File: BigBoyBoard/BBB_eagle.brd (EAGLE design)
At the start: 94 x 87.1 mm, 36 parts, among them Y2 ECS-80-S-4X

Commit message: 1/1 review
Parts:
- moved U$6 1.60 mm to (47.0, 78.7)
- moved U$4 0.83 mm to (46.5, 7.40)
- moved RSH2 0.61 mm to (39.0, 50.7)
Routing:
- net +5VGND: track 167.9 -> 158.1 mm
- net +5V: track 168.8 -> 159.0 mm
- net +12V: track 244.4 -> 237.5 mm
- net GND: track 136.6 -> 134.0 mm, vias 30 -> 31
- net GNDA: track 185.7 -> 183.2 mm
- net +3V3: track 203.9 -> 202.6 mm
- net VCC2: track 27.6 -> 28.2 mm

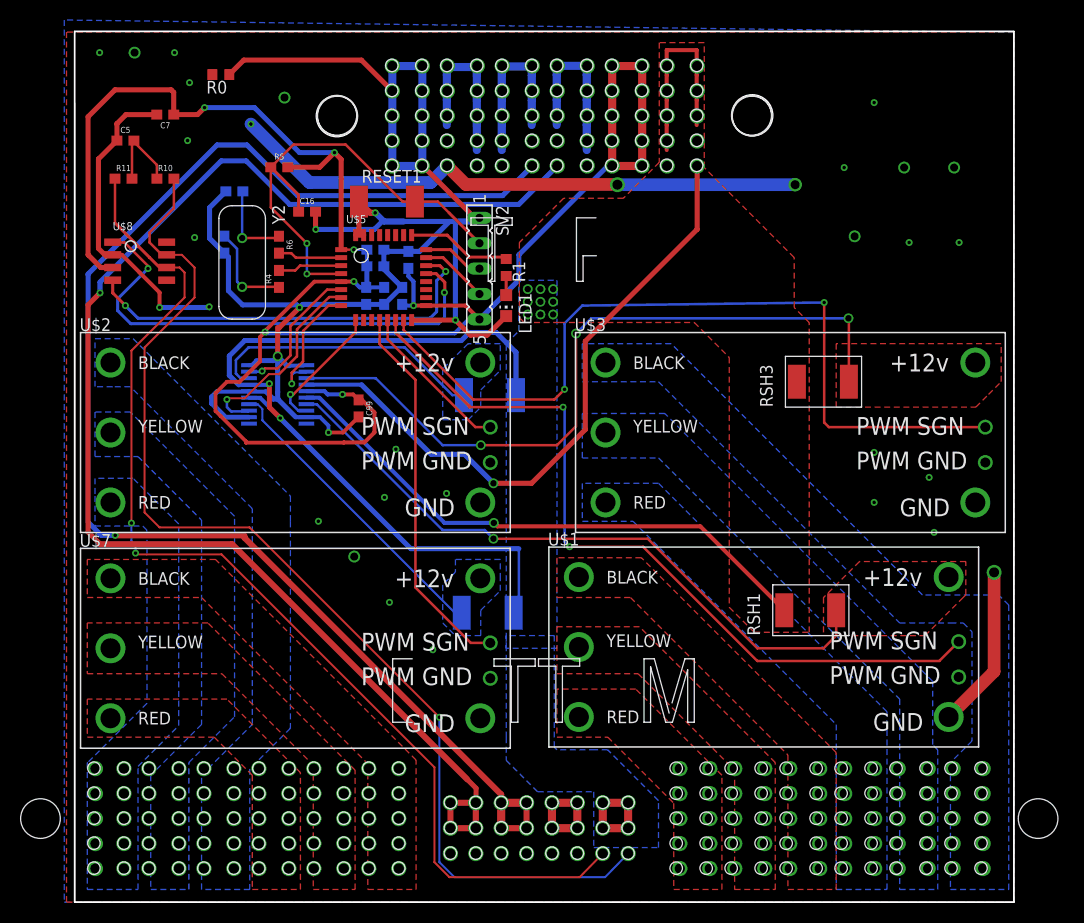
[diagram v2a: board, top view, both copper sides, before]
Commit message: drc errors fixed
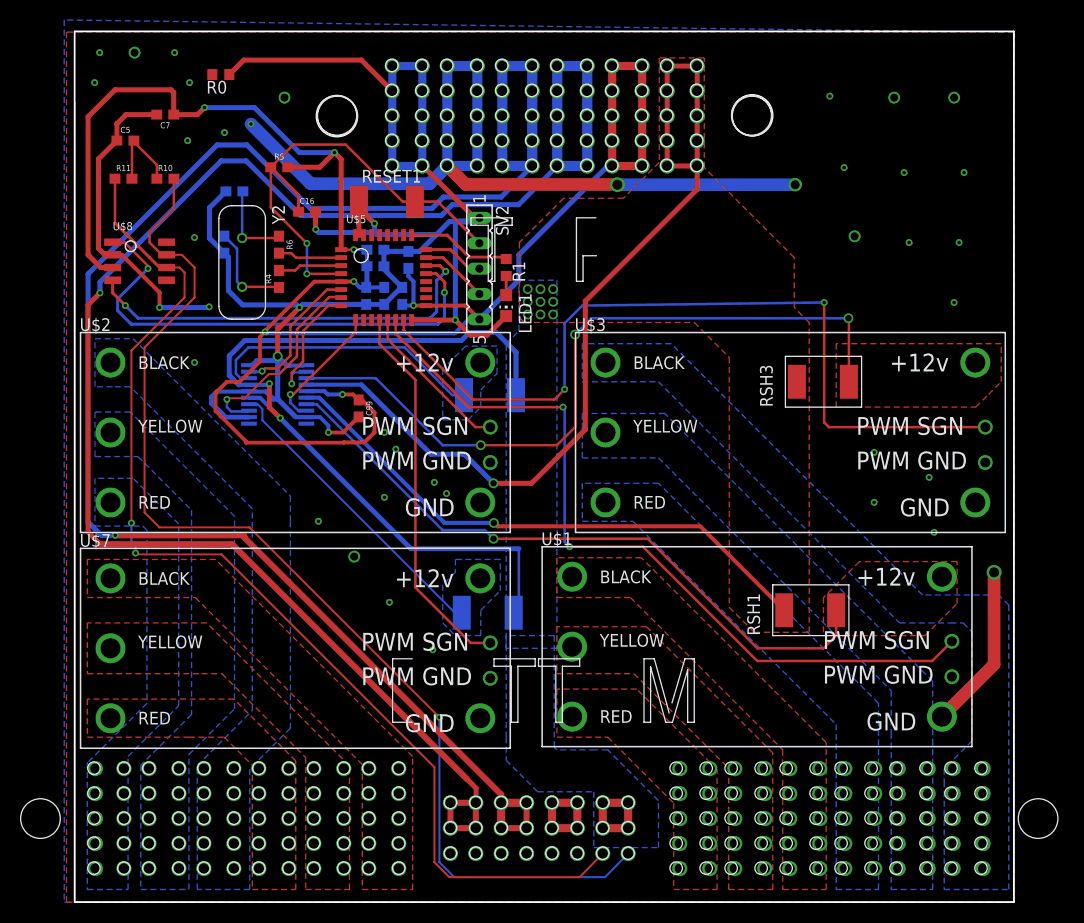
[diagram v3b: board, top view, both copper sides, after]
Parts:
- moved U$1 0.67 mm to (67.8, 25.6)
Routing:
- net +5V: track 159.0 -> 168.7 mm
- net +5VGND: track 158.1 -> 167.7 mm
- net GND: track 134.0 -> 143.2 mm, vias 31 -> 37
- net +12V: track 237.5 -> 243.0 mm
- net GNDA: track 183.2 -> 179.3 mm
- net TIM3_CH3: track 79.9 -> 79.3 mm

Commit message: Update BigBoyBoard/BBB_eagle.brd
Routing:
- net VCC3: track 74.1 -> 73.5 mm
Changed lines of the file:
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@@
 <wire x1="52.842" y1="7.403" x2="55.382" y2="7.403" width="0.8128" layer="1"/>
 <polygon width="0.508" layer="16" thermals="no">
-<vertex x="58.42" y="5.461"/>
-<vertex x="58.42" y="10.16"/>
+<vertex x="56.951" y="6.176"/>
+<vertex x="56.951" y="11.629"/>
 <vertex x="53.34" y="15.24"/>
 <vertex x="52.07" y="15.24"/>
@@
 <vertex x="46.338" y="11.04"/>
 <vertex x="51.943" y="11.04"/>
-<vertex x="51.943" y="5.461"/>
+<vertex x="51.943" y="6.176"/>
 </polygon>
 <contactref element="U$6" pad="R6-6"/>
@@
 <wire x1="32.92" y1="57.25" x2="32.92" y2="58.24" width="0.254" layer="1"/>
 <wire x1="39.878" y1="50.292" x2="32.92" y2="57.25" width="0.254" layer="1"/>
-<wire x1="50.8" y1="59.69" x2="75" y2="60" width="0.254" layer="16"/>
-<via x="75" y="60" extent="1-16" drill="0.35"/>
-<wire x1="75" y1="48" x2="75" y2="60" width="0.254" layer="1"/>
-<wire x1="91.12" y1="47.53" x2="75.47" y2="47.53" width="0.254" layer="1"/>
-<wire x1="75.47" y1="47.53" x2="75" y2="48" width="0.254" layer="1"/>
+<wire x1="91.12" y1="47.53" x2="76.47" y2="47.53" width="0.254" layer="1"/>
+<wire x1="76.47" y1="47.53" x2="76" y2="48" width="0.254" layer="1"/>
+<wire x1="76" y1="48" x2="75" y2="49" width="0.254" layer="1"/>
+<wire x1="50.8" y1="59.69" x2="73.914" y2="59.69" width="0.2032" layer="16"/>
+<via x="74.295" y="59.309" extent="1-16" drill="0.35"/>
+<wire x1="74.295" y1="59.309" x2="74.295" y2="49.705" width="0.2032" layer="1"/>
+<wire x1="74.295" y1="49.705" x2="76" y2="48" width="0.2032" layer="1"/>
+<wire x1="73.914" y1="59.69" x2="74.295" y2="59.309" width="0.2032" layer="16"/>
 </signal>
 <signal name="TIM3_CH3">
@@
 <via x="50.076" y="56.792" extent="1-16" drill="0.635"/>
 <wire x1="50.076" y1="56.792" x2="51.704" y2="58.42" width="0.254" layer="16"/>
-<wire x1="51.704" y1="58.42" x2="77.43" y2="58.42" width="0.254" layer="16"/>
-<via x="77.43" y="58.42" extent="1-16" drill="0.635"/>
-<wire x1="77.43" y1="58.42" x2="77.47" y2="58.38" width="0.254" layer="1"/>
-<wire x1="77.47" y1="58.38" x2="77.47" y2="52.07" width="0.254" layer="1"/>
+<wire x1="51.704" y1="58.42" x2="76.43" y2="58.42" width="0.254" layer="16"/>
+<via x="76.43" y="58.42" extent="1-16" drill="0.635"/>
+<wire x1="76.43" y1="58.42" x2="77.47" y2="57.38" width="0.254" layer="1"/>
+<wire x1="77.47" y1="57.38" x2="77.47" y2="52.07" width="0.254" layer="1"/>
 </signal>
 <signal name="VCC2">
